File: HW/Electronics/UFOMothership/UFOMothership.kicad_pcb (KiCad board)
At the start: 2 copper layers, 140 x 115 mm, 4 parts

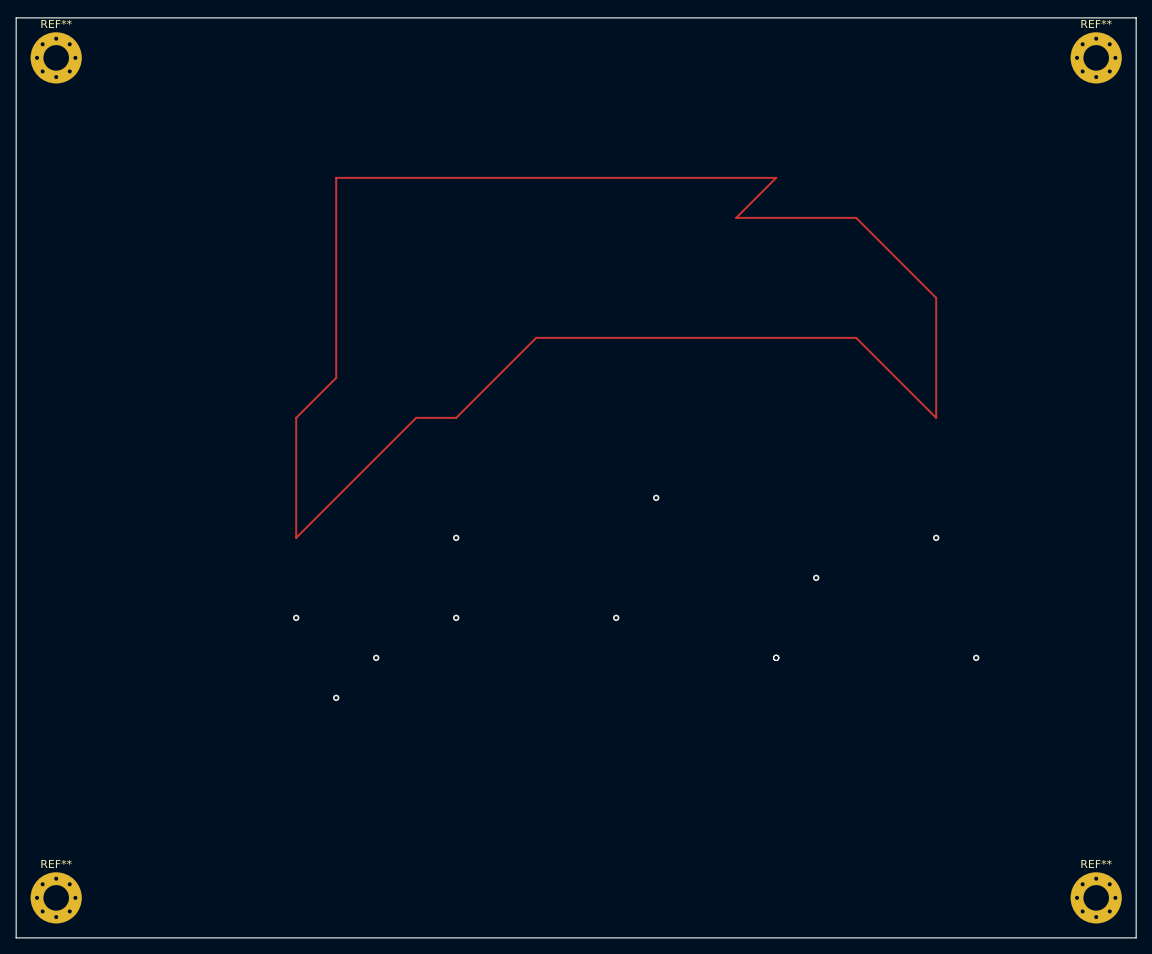
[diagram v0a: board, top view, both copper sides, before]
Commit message: files for manufactured mothership pulsedeck and controldeck
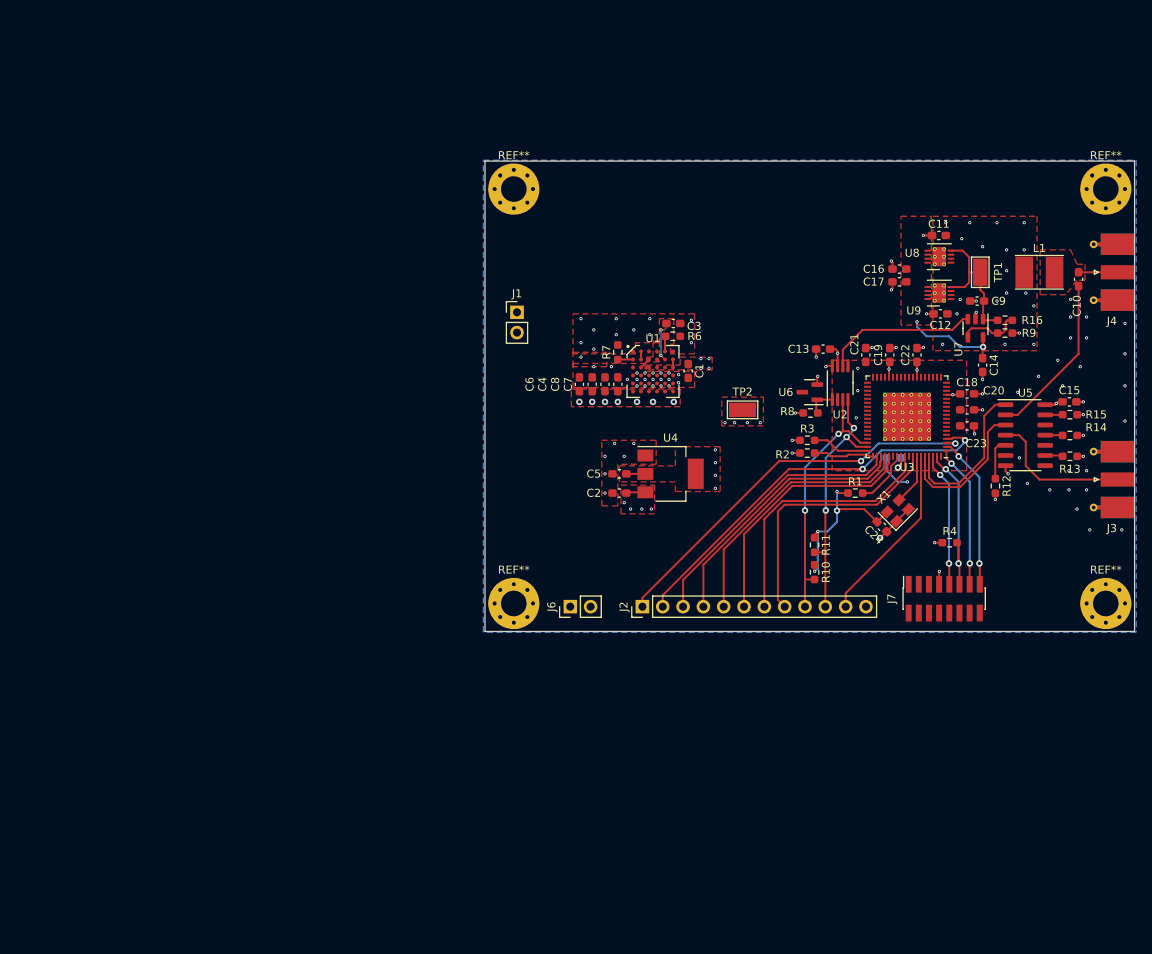
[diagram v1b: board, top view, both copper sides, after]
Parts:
- removed the REF** at (205.0, 40.0)
- removed the REF** at (75.0, 40.0)
- removed the REF** at (75.0, 145.0)
- added C1: C, Capacitor_SMD:C_0603_1608Metric_Pad1.08x0.95mm_HandSolder, F.Cu at (154.0, 79.1)
- added C10: C, Capacitor_SMD:C_0603_1608Metric_Pad1.08x0.95mm_HandSolder, F.Cu at (202.8, 67.7)
- added C11: C, Capacitor_SMD:C_0603_1608Metric_Pad1.08x0.95mm_HandSolder, F.Cu at (185.3, 62.2)
- added C12: C, Capacitor_SMD:C_0603_1608Metric_Pad1.08x0.95mm_HandSolder, F.Cu at (185.5, 72.0)
- added C13: C, Capacitor_SMD:C_0603_1608Metric_Pad1.08x0.95mm_HandSolder, F.Cu at (170.9, 76.4)
- added C14: C, Capacitor_SMD:C_0603_1608Metric_Pad1.08x0.95mm_HandSolder, F.Cu at (190.8, 78.4)
- added C15: C, Capacitor_SMD:C_0603_1608Metric_Pad1.08x0.95mm_HandSolder, F.Cu at (201.7, 83.0)
- added C16: C, Capacitor_SMD:C_0603_1608Metric_Pad1.08x0.95mm_HandSolder, F.Cu at (180.4, 66.4)
- added C17: C, Capacitor_SMD:C_0603_1608Metric_Pad1.08x0.95mm_HandSolder, F.Cu at (180.4, 68.0)
- added C18: C, Capacitor_SMD:C_0603_1608Metric_Pad1.08x0.95mm_HandSolder, F.Cu at (188.9, 82.0)
- added C19: C, Capacitor_SMD:C_0603_1608Metric_Pad1.08x0.95mm_HandSolder, F.Cu at (179.2, 77.1)
- added C2: C, Capacitor_SMD:C_0603_1608Metric_Pad1.08x0.95mm_HandSolder, F.Cu at (145.4, 94.4)
- added C20: C, Capacitor_SMD:C_0603_1608Metric_Pad1.08x0.95mm_HandSolder, F.Cu at (188.9, 84.0)
- added C21: C, Capacitor_SMD:C_0603_1608Metric_Pad1.08x0.95mm_HandSolder, F.Cu at (176.2, 77.1)
- added C22: C, Capacitor_SMD:C_0603_1608Metric_Pad1.08x0.95mm_HandSolder, F.Cu at (182.6, 77.1)
- added C23: C, Capacitor_SMD:C_0603_1608Metric_Pad1.08x0.95mm_HandSolder, F.Cu at (188.9, 86.0)
- added C24: C, Capacitor_SMD:C_0603_1608Metric_Pad1.08x0.95mm_HandSolder, F.Cu at (178.2, 98.6)
- added C3: C, Capacitor_SMD:C_0603_1608Metric_Pad1.08x0.95mm_HandSolder, F.Cu at (152.1, 73.2)
- added C4: C, Capacitor_SMD:C_0603_1608Metric_Pad1.08x0.95mm_HandSolder, F.Cu at (142.0, 80.8)
- added C5: C, Capacitor_SMD:C_0603_1608Metric_Pad1.08x0.95mm_HandSolder, F.Cu at (145.4, 92.0)
- added C6: C, Capacitor_SMD:C_0603_1608Metric_Pad1.08x0.95mm_HandSolder, F.Cu at (140.4, 80.8)
- added C7: C, Capacitor_SMD:C_0603_1608Metric_Pad1.08x0.95mm_HandSolder, F.Cu at (145.2, 80.8)
- added C8: C, Capacitor_SMD:C_0603_1608Metric_Pad1.08x0.95mm_HandSolder, F.Cu at (143.6, 80.8)
- added C9: C, Capacitor_SMD:C_0603_1608Metric_Pad1.08x0.95mm_HandSolder, F.Cu at (190.1, 70.4)
- added J1: Conn_01x02, Connector_PinHeader_2.54mm:PinHeader_1x02_P2.54mm_Vertical, F.Cu at (132.6, 71.8)
- added J2: Conn_01x12, Connector_PinHeader_2.54mm:PinHeader_1x12_P2.54mm_Vertical, F.Cu at (148.3, 108.6)
- added J3: Conn_Coaxial, Connector_Coaxial:SMA_Molex_73251-2120_EdgeMount_Horizontal, F.Cu at (207.7, 92.7)
- added J4: Conn_Coaxial, Connector_Coaxial:SMA_Molex_73251-2120_EdgeMount_Horizontal, F.Cu at (207.7, 66.8)
- added J6: Conn_01x02, Connector_PinHeader_2.54mm:PinHeader_1x02_P2.54mm_Vertical, F.Cu at (139.3, 108.6)
- added J7: Conn_02x08_Odd_Even, Connector_PinSocket_1.27mm:PinSocket_2x08_P1.27mm_Vertical_SMD, F.Cu at (186.0, 107.6)
- added L1: L, Inductor_SMD:L_Taiyo-Yuden_NR-40xx_HandSoldering, F.Cu at (197.9, 66.8)
- added R1: R, Resistor_SMD:R_0603_1608Metric_Pad0.98x0.95mm_HandSolder, F.Cu at (174.9, 94.4)
- added R10: R, Resistor_SMD:R_0603_1608Metric_Pad0.98x0.95mm_HandSolder, F.Cu at (169.8, 104.3)
- added R11: R, Resistor_SMD:R_0603_1608Metric_Pad0.98x0.95mm_HandSolder, F.Cu at (169.8, 100.9)
- added R12: R, Resistor_SMD:R_0603_1608Metric_Pad0.98x0.95mm_HandSolder, F.Cu at (192.4, 93.5)
- added R13: R, Resistor_SMD:R_0603_1608Metric_Pad0.98x0.95mm_HandSolder, F.Cu at (201.7, 89.8)
- added R14: R, Resistor_SMD:R_0603_1608Metric_Pad0.98x0.95mm_HandSolder, F.Cu at (201.7, 87.2)
- added R15: R, Resistor_SMD:R_0603_1608Metric_Pad0.98x0.95mm_HandSolder, F.Cu at (201.7, 84.6)
- added R16: R, Resistor_SMD:R_0603_1608Metric_Pad0.98x0.95mm_HandSolder, F.Cu at (193.6, 72.8)
- added R2: R, Resistor_SMD:R_0603_1608Metric_Pad0.98x0.95mm_HandSolder, F.Cu at (168.9, 89.4)
- added R3: R, Resistor_SMD:R_0603_1608Metric_Pad0.98x0.95mm_HandSolder, F.Cu at (168.9, 87.8)
- added R4: R, Resistor_SMD:R_0603_1608Metric_Pad0.98x0.95mm_HandSolder, F.Cu at (186.7, 100.6)
- added R5: R, Resistor_SMD:R_0603_1608Metric_Pad0.98x0.95mm_HandSolder, B.Cu at (179.7, 90.0)
- added R6: R, Resistor_SMD:R_0603_1608Metric_Pad0.98x0.95mm_HandSolder, F.Cu at (152.1, 74.8)
- added R7: R, Resistor_SMD:R_0603_1608Metric_Pad0.98x0.95mm_HandSolder, F.Cu at (145.2, 76.8)
- added R8: R, Resistor_SMD:R_0603_1608Metric_Pad0.98x0.95mm_HandSolder, F.Cu at (169.3, 84.4)
- added R9: R, Resistor_SMD:R_0603_1608Metric_Pad0.98x0.95mm_HandSolder, F.Cu at (193.6, 74.4)
- added REF**: MountingHole_3.2mm_M3_Pad_Via, MountingHole:MountingHole_3.2mm_M3_Pad_Via, F.Cu at (206.2, 56.4)
- added REF**: MountingHole_3.2mm_M3_Pad_Via, MountingHole:MountingHole_3.2mm_M3_Pad_Via, F.Cu at (132.2, 108.2)
- added REF**: MountingHole_3.2mm_M3_Pad_Via, MountingHole:MountingHole_3.2mm_M3_Pad_Via, F.Cu at (132.2, 56.4)
- added TP1: TestPoint, TestPoint:TestPoint_Keystone_5015_Micro-Minature, F.Cu at (190.5, 66.8)
- added TP2: TestPoint, TestPoint:TestPoint_Keystone_5015_Micro-Minature, F.Cu at (160.8, 84.0)
- added U1: LTM8065, MPS:BGA-36_6x6_6.25x6.25mm, F.Cu at (149.6, 79.2)
- added U2: MAX5215, Package_SO:MSOP-8_3x3mm_P0.65mm, F.Cu at (173.0, 80.6)
- added U3: UFOControlDeck-rescue_LCMXO3D-4300ZC-3SG72I-MachXO3D, Package_DFN_QFN:QFN-72-1EP_10x10mm_P0.5mm_EP6x6mm_ThermalVias, F.Cu at (181.3, 84.9)
- added U4: LD1117S33TR_SOT223, Package_TO_SOT_SMD:SOT-223-3_TabPin2, F.Cu at (151.8, 92.0)
- added U5: SN74AS1034AD, Package_SO:SOIC-14_3.9x8.7mm_P1.27mm, F.Cu at (196.2, 87.2)
- added U6: LM4040DBZ-3, Package_TO_SOT_SMD:SOT-23, F.Cu at (169.2, 81.8)
- added U7: ADA4622-1, Package_TO_SOT_SMD:SOT-23-5, F.Cu at (189.9, 73.8)
- added U8: LT3082IDD, Package_DFN_QFN:DFN-8-1EP_3x3mm_P0.5mm_EP1.65x2.38mm_ThermalVias, F.Cu at (185.4, 64.9)
- added U9: LT3082IDD, Package_DFN_QFN:DFN-8-1EP_3x3mm_P0.5mm_EP1.65x2.38mm_ThermalVias, F.Cu at (185.4, 69.4)
- added X1: ASE-xxxMHz, Oscillator:Oscillator_SMD_Abracon_ASE-4Pin_3.2x2.5mm, F.Cu at (180.2, 96.6)
- moved REF** 36.8 mm to (206.2, 108.2)
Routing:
- net (no net): track 247.8 -> 0.00 mm, vias 12 -> 0
- net /GPIO1: track 0.00 -> 49.9 mm, vias 0 -> 2
- net /GPIO0: track 0.00 -> 49.4 mm, vias 0 -> 2
- net +3.3V: track 0.00 -> 41.3 mm, vias 0 -> 19
- net /GPIO2: track 0.00 -> 34.6 mm
- net /GPIO3: track 0.00 -> 33.7 mm
- net /SCL: track 0.00 -> 33.6 mm, vias 0 -> 2
- net /GPIO4: track 0.00 -> 32.9 mm
- net /GPIO7: track 0.00 -> 32.9 mm
- net /GPIO6: track 0.00 -> 32.9 mm
- net /SDA: track 0.00 -> 32.2 mm, vias 0 -> 3
- net /GPIO5: track 0.00 -> 32.1 mm
- net GND: track 0.00 -> 30.3 mm, vias 0 -> 92
- net /TRIGGER_IN: track 0.00 -> 22.7 mm
- net /TRIGGER: track 0.00 -> 20.8 mm
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- added copper zone on F.Cu, net +3.3V
- added copper zone on In2.Cu, net +3.3V
- added copper zone on F.Cu, net +5V
- added copper zone on In2.Cu, net +5V
- added copper zone on F.Cu, net +VDC
- added copper zone on In2.Cu, net +VDC
- added copper zone on F.Cu, net /BIAS
- added copper zone on In2.Cu, net /BIAS
- added copper zone on F.Cu, net /TRIG+BIAS
- added copper zone on B.Cu, net GND
- added copper zone on F.Cu, net GND
- added copper zone on In1.Cu, net GND
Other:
- board size 140 x 115 mm -> 81.2 x 58.8 mm
- copper layers 2 -> 4
- net class Default removed
